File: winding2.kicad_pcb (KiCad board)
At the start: 2 copper layers, 103.4 x 74.2 mm, 19 parts, among them J1 Screw_Terminal_2_P5.00mm, J2 Limit Switches, J3 Screw Stepper, J4 Main Stepper, J5 RPM & ESC, J6 Barrel_Jack_PTH_Slot, J7 ESC XT60-F, J8 ARDUINO PROG., M1 Push_Button_W12mm, SW1 RotaryEncoder_Switch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

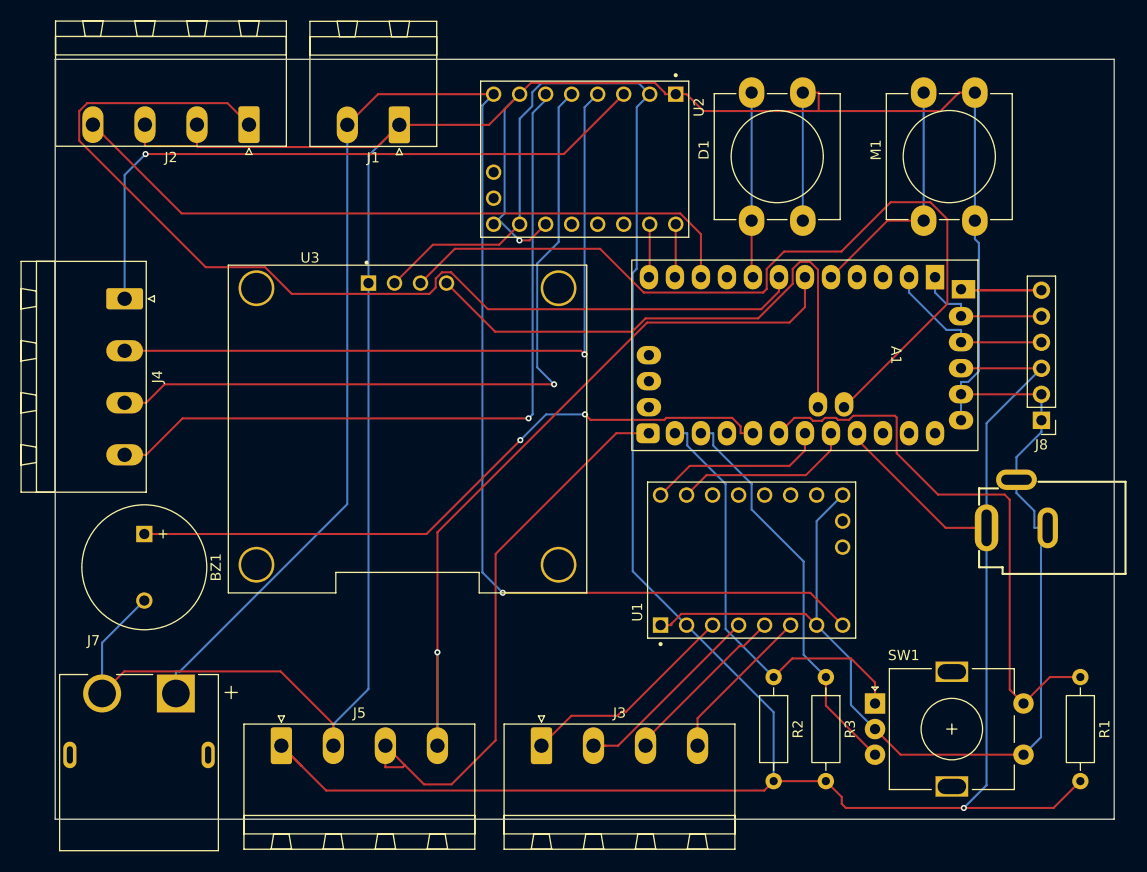
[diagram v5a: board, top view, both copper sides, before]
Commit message: Manual routing with ground plan - v0.0
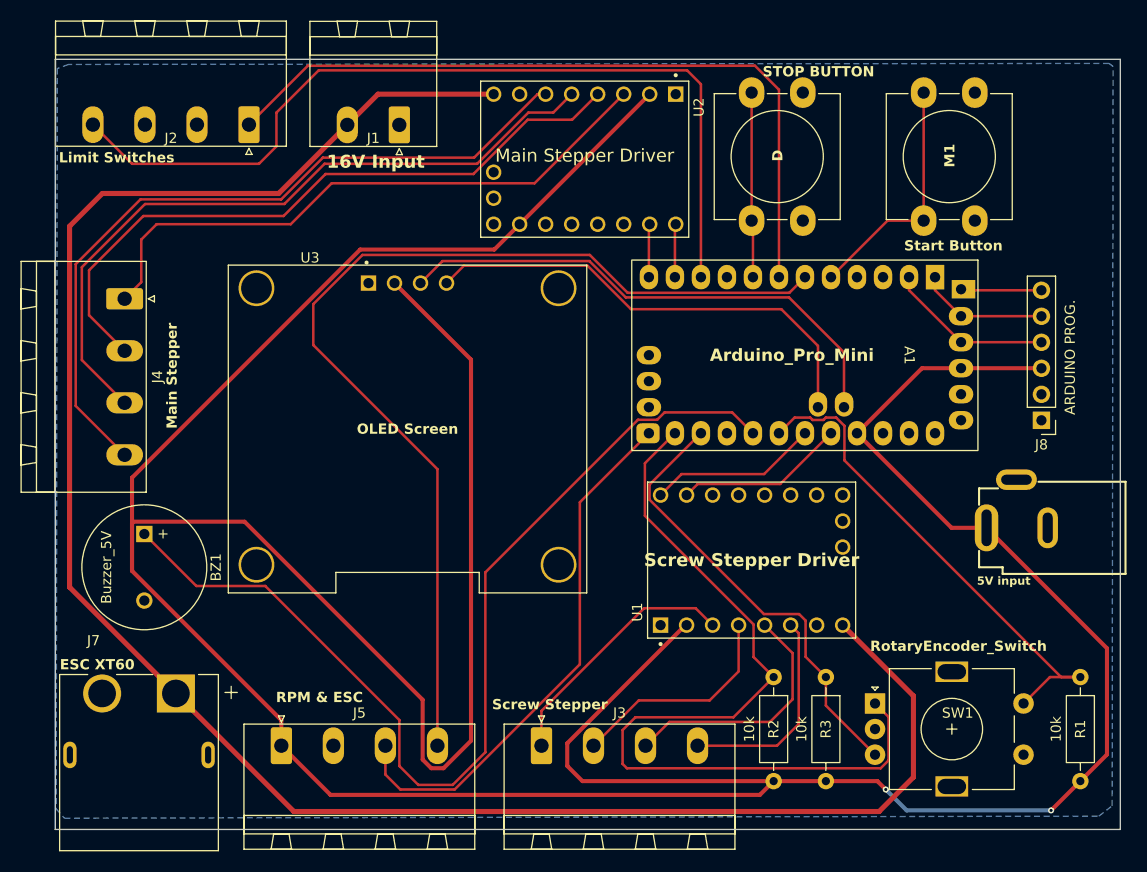
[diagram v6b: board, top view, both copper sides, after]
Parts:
- A1: value Arduino_Pro_Mini(with_programming_pins) -> Arduino_Pro_Mini
- J6: value Barrel_Jack_PTH_Slot -> 5V input
- J7: value ESC XT60-F -> ESC XT60
- STOP BUTTON: renamed from D1
- Start Button: renamed from M1
- U3: value DM-OLED096-636 -> OLED Screen
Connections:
- net /16V renamed +16V
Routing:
- net GND: track 365.5 -> 0.00 mm, vias 1 -> 0
- net 5V: track 271.5 -> 388.5 mm, vias 1 -> 2
- net /ENCODER_A: track 42.2 -> 83.0 mm
- net /BUZZ-A0: track 65.6 -> 98.4 mm, vias 2 -> 0
- net /OLED-A5: track 82.6 -> 51.3 mm
- net +16V: track 162.7 -> 192.6 mm, vias 1 -> 0
- net /limit1: track 100.2 -> 73.4 mm
- net /RPM: track 77.9 -> 100.3 mm, vias 1 -> 0
- net /limit2: track 68.0 -> 86.1 mm
- net /OLED-A4: track 55.7 -> 46.2 mm
- net /S2A: track 16.8 -> 24.6 mm
- net /ENCODER_SW: track 56.2 -> 49.3 mm
- net /ENCODER_B: track 39.1 -> 44.6 mm
- net /S2B: track 15.5 -> 20.7 mm
- net /M1A: track 71.0 -> 66.1 mm, vias 1 -> 0
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- added copper zone on B.Cu, net GND
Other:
- board size 103.4 x 74.2 mm -> 104 x 75.2 mm

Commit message: releases folder added with v0.0 greber files
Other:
- board text added: "version 0.0"
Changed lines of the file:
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@@
 		)
 		(property "Value" "5V input"
-			(at -6.9087 5.6513 0)
+			(at -6.9087 6.1013 0)
 			(layer "F.SilkS")
 			(effects
 				(font
-					(size 0.8 0.8)
-					(thickness 0.2)
+					(size 1 1)
+					(thickness 0.25)
 					(bold yes)
 				)
@@
 		(layer "Edge.Cuts")
 	)
+	(gr_text "version 0.0"
+		(at 149.75 104.75 0)
+		(layer "B.SilkS" knockout)
+		(effects
+			(font
+				(size 3 3)
+				(thickness 0.75)
+				(bold yes)
+			)
+			(justify bottom mirror)
+		)
+	)
+	(dimension
+		(type aligned)
+		(layer "F.SilkS")
+		(pts
+			(xy 219.2 149.6) (xy 115.2 149.6)
+		)
+		(height -6.65)
+		(format
+			(prefix "")
+			(suffix "")
+			(units 3)
+			(units_format 0)
+			(precision 4)
+			(suppress_zeroes yes)
+		)
+		(style
+			(thickness 0.1)
+			(arrow_length 1.27)
+			(text_position_mode 0)
+			(arrow_direction outward)
+			(extension_height 0.58642)
+			(extension_offset 0.5)
+			(keep_text_aligned yes)
+		)
+		(gr_text "104"
+			(at 167.2 155.15 0)
+			(layer "F.SilkS")
+			(effects
+				(font
+					(size 1 1)
+					(thickness 0.1)
+				)
+			)
+		)
+	)
+	(dimension
+		(type aligned)
+		(layer "F.SilkS")
+		(pts
+			(xy 219.2 74.4) (xy 219.2 149.6)
+		)
+		(height -9.05)
+		(format
+			(prefix "")
+			(suffix "")
+			(units 3)
+			(units_format 0)
+			(precision 4)
+			(suppress_zeroes yes)
+		)
+		(style
+			(thickness 0.1)
+			(arrow_length 1.27)
+			(text_position_mode 0)
+			(arrow_direction outward)
+			(extension_height 0.58642)
+			(extension_offset 0.5)
+			(keep_text_aligned yes)
+		)
+		(gr_text "75.2"
+			(at 227.15 112 90)
+			(layer "F.SilkS")
+			(effects
+				(font
+					(size 1 1)
+					(thickness 0.1)
+				)
+			)
+		)
+	)
 	(segment
